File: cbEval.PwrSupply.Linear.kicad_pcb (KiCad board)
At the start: 2 copper layers, 35 x 109 mm, 34 parts, among them J1 CAL.CT3151V1-0, J11 Bergstik-II_6, J12 Header.Hor.2x8.9-103326-0-08, J13 Header.Hor.2x8.9-103326-0-08, J2 CAL.CT3151V1-2, J3 Socket.Hor.2x8.1-5535512-8, J4 Socket.Hor.2x8.1-5535512-8, U1 MIC29151-5.0WU, U2 MIC29151-3.3WU, U3 DS1834AS+

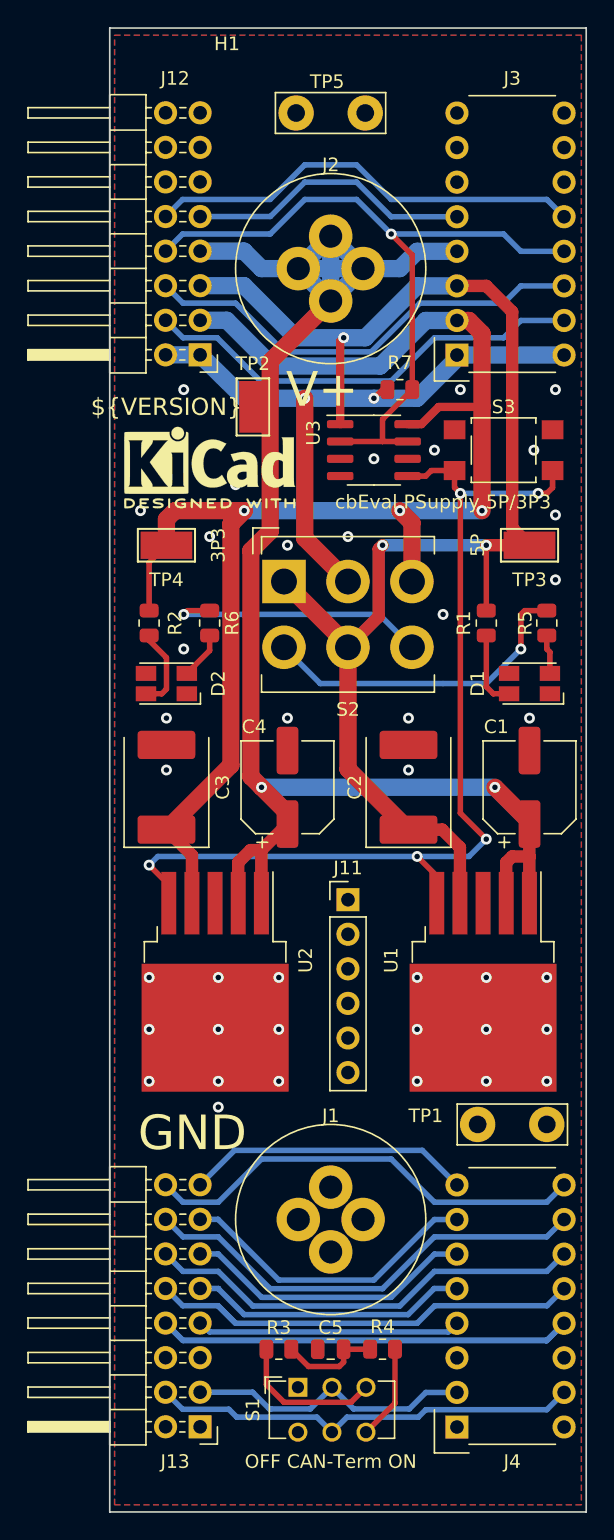
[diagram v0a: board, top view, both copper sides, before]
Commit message: Position von Steckern ausgerückt, SilkScreen von Steckern verändert
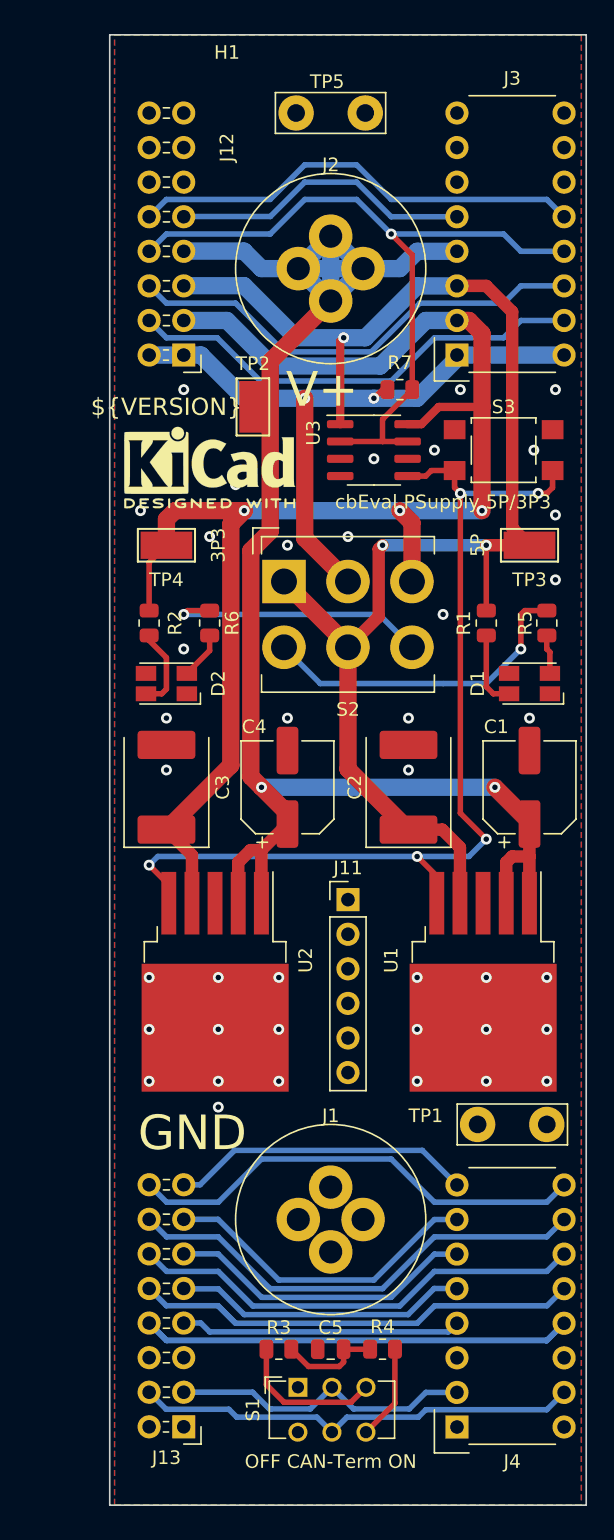
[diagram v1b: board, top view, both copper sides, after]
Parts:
- J12, J13: footprint Connector_PinHeader_2.54mm:PinHeader_2x08_P2.54mm_Horizontal -> BTech.PinHeader.2-54mm:PinHeader_2x08_P2.54mm_Horizontal
- moved J12 1.21 mm to (134.0, 70.5)
- moved J13 1.20 mm to (134.0, 149.2)
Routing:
- net /Reserved1: track 60.7 -> 63.1 mm
- net VCC: track 48.1 -> 49.3 mm
- net ~{RESET}: track 54.2 -> 55.4 mm
- net /I2C-SCL: track 32.4 -> 33.6 mm
- net +5V: track 105.6 -> 106.8 mm
- net /I2C-SDA: track 21.0 -> 22.2 mm
- net +VDC: track 123.4 -> 124.6 mm
- net /SPI-~{CE}: track 32.4 -> 33.6 mm
- net /SPI-MRST: track 33.2 -> 34.4 mm
- net /SPI-ADR1: track 33.5 -> 34.7 mm
- net /One-Wire: track 33.0 -> 34.2 mm
- net /CAN-L: track 31.7 -> 32.9 mm
- net /SPI-CLK: track 21.5 -> 22.7 mm
- net /SPI-ADR2: track 21.0 -> 22.2 mm
- net /SPI-ADR0: track 22.6 -> 23.8 mm
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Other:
- board size 35 x 109 mm -> 35 x 108 mm

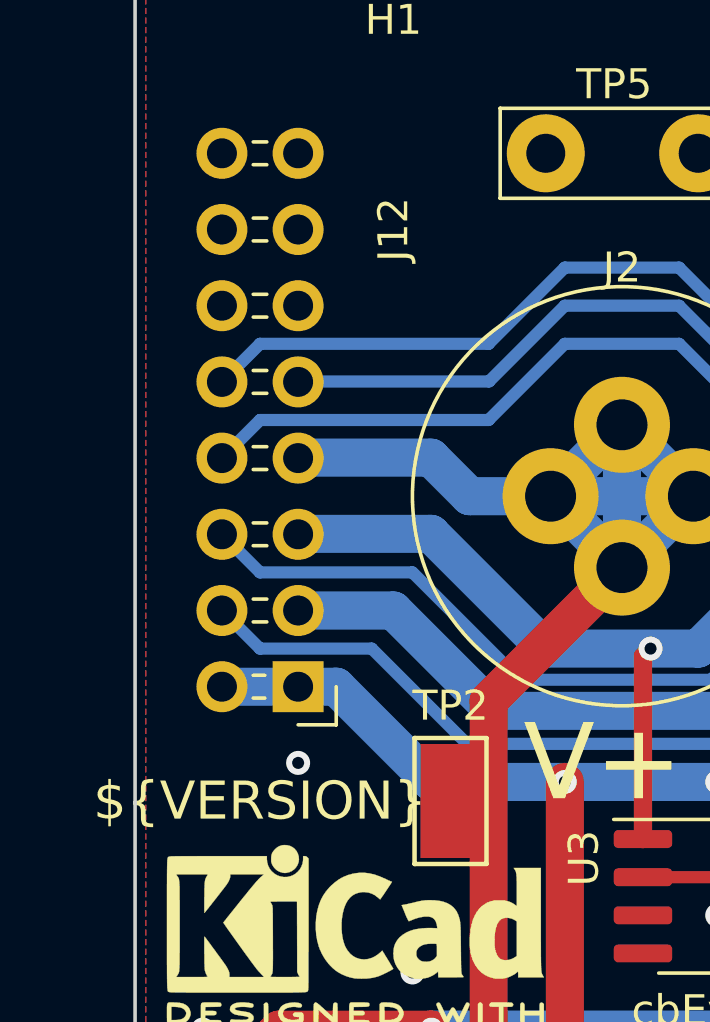
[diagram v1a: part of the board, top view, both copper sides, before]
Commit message: Widerstandswerte zur Ansteuerung derngrünen LEDs auf 560 Ohm verringert. Neue Version 1.1.1
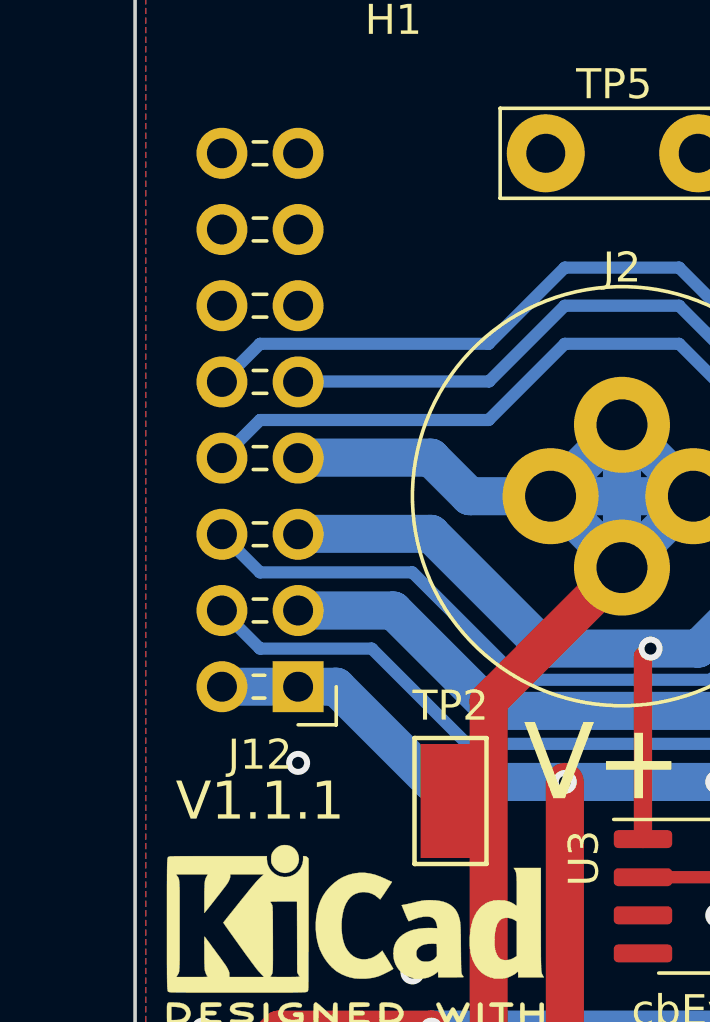
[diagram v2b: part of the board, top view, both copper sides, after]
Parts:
- R5, R6: value 649R -> 560R
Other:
- board text added: "V1.1.1"
- board text added: "cbEval PSupply 5P/3P3"
- board text removed: "${TITLE}"
- board text removed: "${VERSION}"
